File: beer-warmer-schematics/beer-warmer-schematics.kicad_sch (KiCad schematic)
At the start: 38 parts, among them J1 USB_C_Receptacle_USB2.0_14P, J2 Screw_Terminal_01x02, J3 Conn_01x07_Socket, J4 Conn_01x07_Socket, J5 Conn_01x04_Pin, J6 Screw_Terminal_01x03, Q1 AOD4184A, U2 LM2596S-5, U3 CH224K, U4 INA219AxDCN

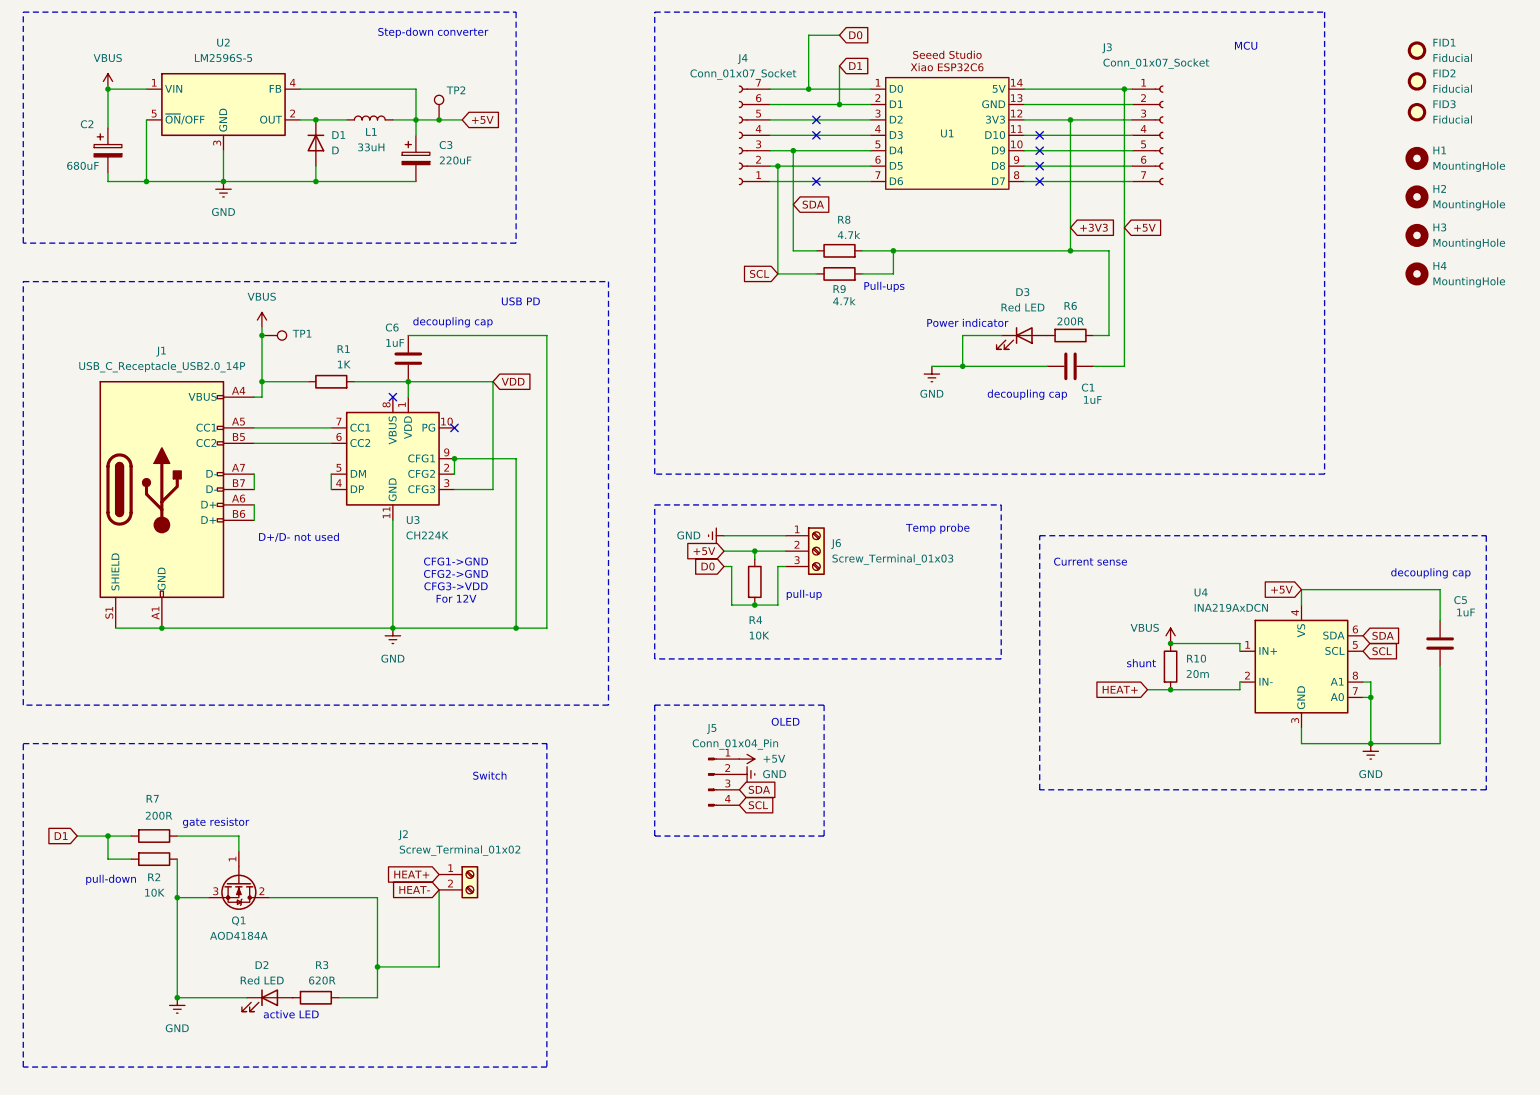
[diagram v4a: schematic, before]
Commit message: fix active led, bottom silkscreen
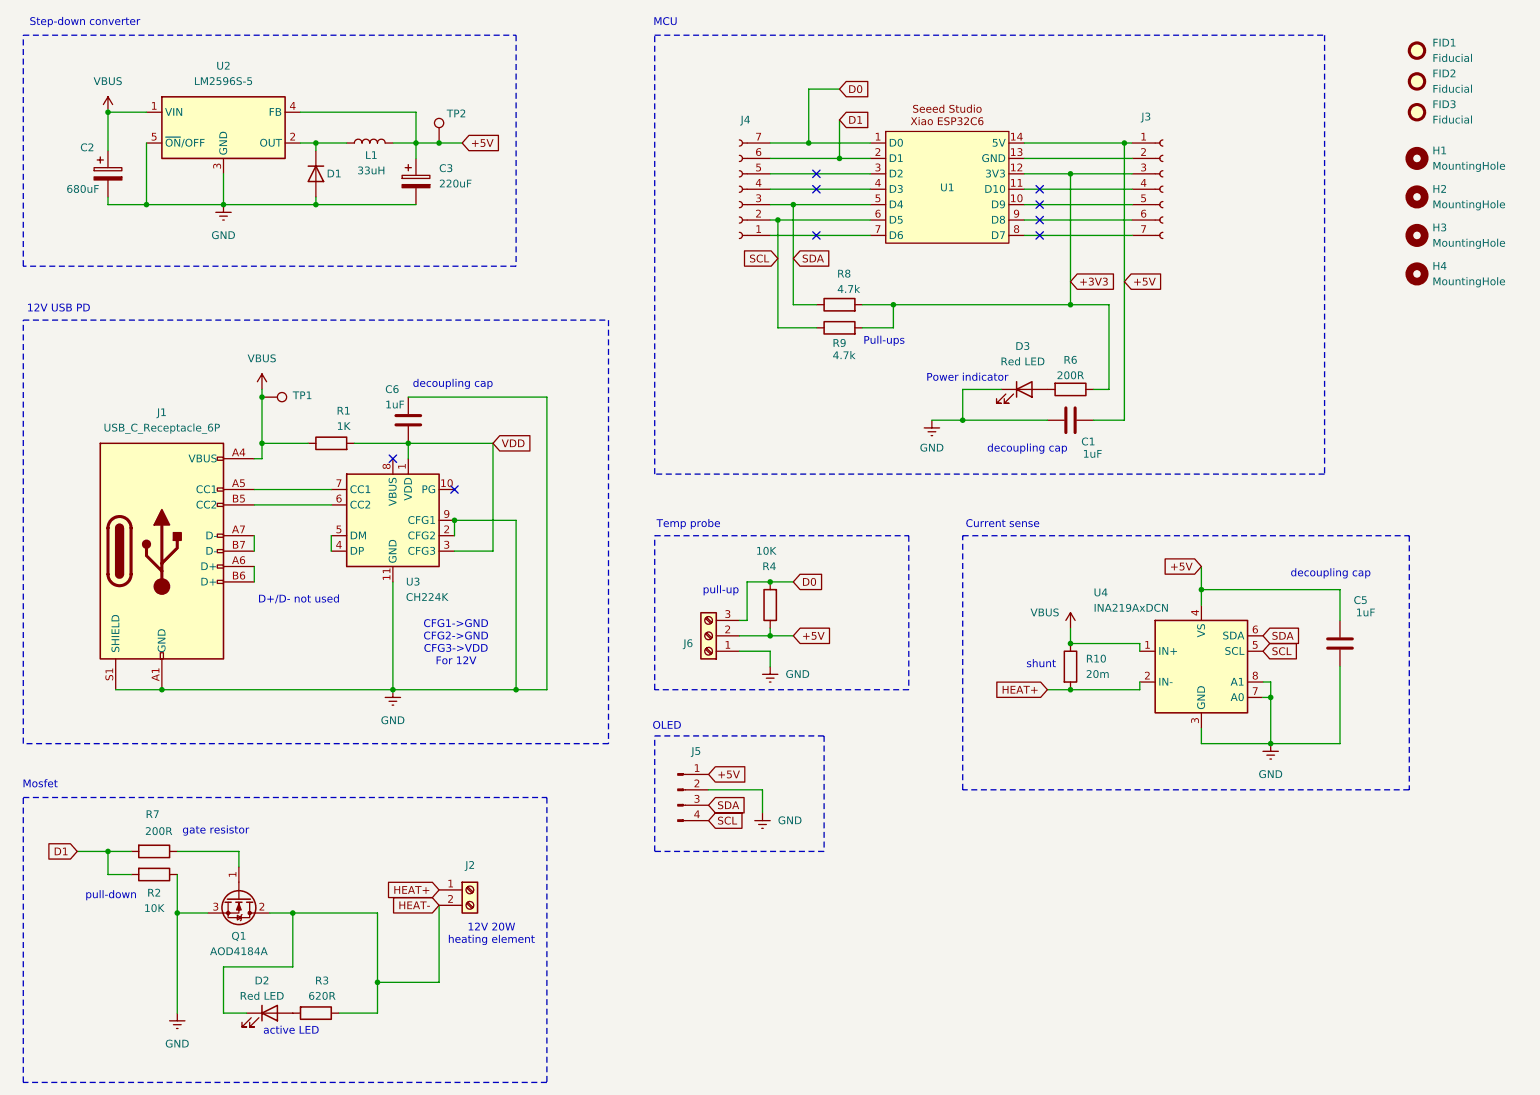
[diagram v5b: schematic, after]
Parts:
- J1: value USB_C_Receptacle_USB2.0_14P -> USB_C_Receptacle_6P
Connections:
- net GND: no longer D2.1 (K)
- net HEAT-: now also D2.1 (K)
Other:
- note added: "12V 20W heating element"
- note added: "12V USB PD"
- note added: "Mosfet"
- note removed: "Switch"
- note removed: "USB PD"
- moved on the sheet: C1, C2, C3, C5, C6, D1, D2, D3, J1, J2, J3, J4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

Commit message: incorporated some feedback
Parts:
- J1: symbol Connector:USB_C_Receptacle_USB2.0_14P -> Connector:USB_C_Receptacle_PowerOnly_6P
- J3, J4: symbol Connector:Conn_01x07_Socket -> Connector_Generic:Conn_01x07
- J5: symbol Connector:Conn_01x04_Pin -> Connector_Generic:Conn_01x04
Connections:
- net D1: now also R2.1; no longer R2.2
- net GND: now also J3.2 (Pin_2), R2.2, U1.13 (GND); no longer J1.A1 (GND), J1.B1 (GND), R2.1
- net SCL: now also R8.1; no longer R9.1
- net SDA: now also R9.1; no longer R8.1
- net VBUS: no longer J1.A4 (VBUS), J1.B4 (VBUS)
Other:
- note removed: "D+/D- not used"
- moved on the sheet: C1, C5, C6, D3, R2, R6, R8, R9, U1

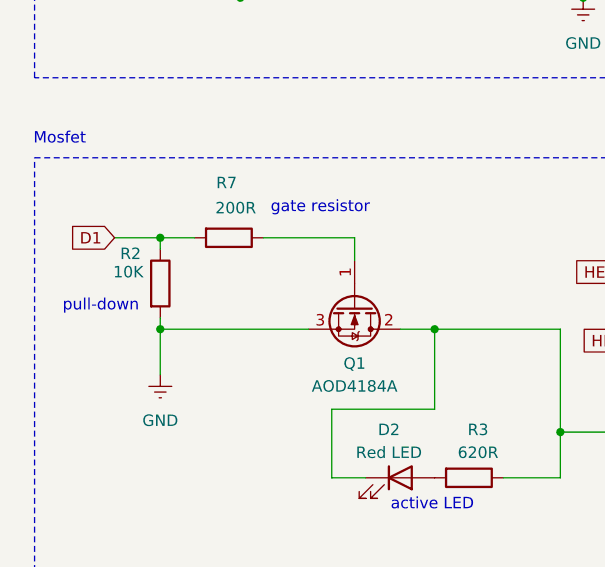
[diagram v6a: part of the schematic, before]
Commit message: low side driver
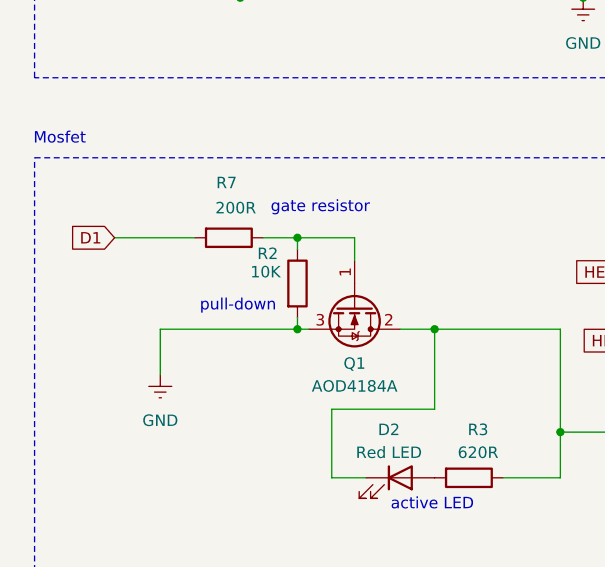
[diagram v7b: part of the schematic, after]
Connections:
- net D1: no longer R2.1
- net at Q1.1 (G), R7.1: now also R2.1
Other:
- moved on the sheet: R2
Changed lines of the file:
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@@
 	(text "pull-down"
 		(exclude_from_sim no)
-		(at 35.306 163.83 0)
+		(at 50.546 163.83 0)
 		(effects
 			(font
@@
 	)
 	(junction
+		(at 57.15 166.37)
+		(diameter 0)
+		(color 0 0 0 0)
+	)
+	(junction
 		(at 96.52 39.37)
 		(diameter 0)
@@
 	)
 	(junction
-		(at 41.91 166.37)
-		(diameter 0)
-		(color 0 0 0 0)
-	)
-	(junction
 		(at 200.66 129.54)
 		(diameter 0)
@@
 	)
 	(junction
-		(at 41.91 156.21)
-		(diameter 0)
-		(color 0 0 0 0)
-	)
-	(junction
 		(at 92.71 39.37)
 		(diameter 0)
@@
 	(junction
 		(at 222.25 113.03)
+		(diameter 0)
+		(color 0 0 0 0)
+	)
+	(junction
+		(at 57.15 156.21)
 		(diameter 0)
 		(color 0 0 0 0)
@@
 	(wire
 		(pts
-			(xy 41.91 165.1) (xy 41.91 166.37)
+			(xy 57.15 165.1) (xy 57.15 166.37)
 		)
 		(stroke
@@
 	(wire
 		(pts
-			(xy 53.34 156.21) (xy 63.5 156.21)
+			(xy 53.34 156.21) (xy 57.15 156.21)
+		)
+		(stroke
+			(width 0)
+			(type default)
+		)
+	)
+	(wire
+		(pts
+			(xy 57.15 156.21) (xy 63.5 156.21)
 		)
 		(stroke
@@
 	(wire
 		(pts
-			(xy 36.83 156.21) (xy 41.91 156.21)
+			(xy 36.83 156.21) (xy 45.72 156.21)
 		)
 		(stroke
@@
 	(wire
 		(pts
-			(xy 41.91 156.21) (xy 45.72 156.21)
-		)
-		(stroke
-			(width 0)
-			(type default)
-		)
-	)
-	(wire
-		(pts
 			(xy 69.85 107.95) (xy 69.85 96.52)
 		)
@@
 	(wire
 		(pts
+			(xy 57.15 166.37) (xy 58.42 166.37)
+		)
+		(stroke
+			(width 0)
+			(type default)
+		)
+	)
+	(wire
+		(pts
 			(xy 82.55 88.9) (xy 91.44 88.9)
 		)
@@
 	(wire
 		(pts
-			(xy 41.91 156.21) (xy 41.91 157.48)
-		)
-		(stroke
-			(width 0)
-			(type default)
-		)
-	)
-	(wire
-		(pts
-			(xy 41.91 166.37) (xy 58.42 166.37)
+			(xy 57.15 156.21) (xy 57.15 157.48)
+		)
+		(stroke
+			(width 0)
+			(type default)
+		)
+	)
+	(wire
+		(pts
+			(xy 41.91 166.37) (xy 57.15 166.37)
 		)
 		(stroke
@@
 	(symbol
 		(lib_id "Device:R")
-		(at 41.91 161.29 0)
+		(at 57.15 161.29 0)
 		(unit 1)
 		(exclude_from_sim no)
@@
 		(dnp no)
 		(property "Reference" "R2"
-			(at 38.608 157.988 0)
+			(at 53.848 157.988 0)
 			(effects
 				(font
@@
 		)
 		(property "Value" "10K"
-			(at 38.354 160.02 0)
+			(at 53.594 160.02 0)
 			(effects
 				(font
@@
 		)
 		(property "Footprint" "Resistor_SMD:R_0603_1608Metric"
-			(at 40.132 161.29 90)
+			(at 55.372 161.29 90)
 			(effects
 				(font
@@
 		)
 		(property "Datasheet" "~"
-			(at 41.91 161.29 0)
+			(at 57.15 161.29 0)
 			(effects
 				(font
@@
 		)
 		(property "Description" "Resistor"
-			(at 41.91 161.29 0)
+			(at 57.15 161.29 0)
 			(effects
 				(font
@@
 		)
 		(property "LCSC" "C15401"
-			(at 41.91 161.29 90)
-			(effects
-				(font
+			(at 57.15 161.29 90)
+			(effects
+				(font

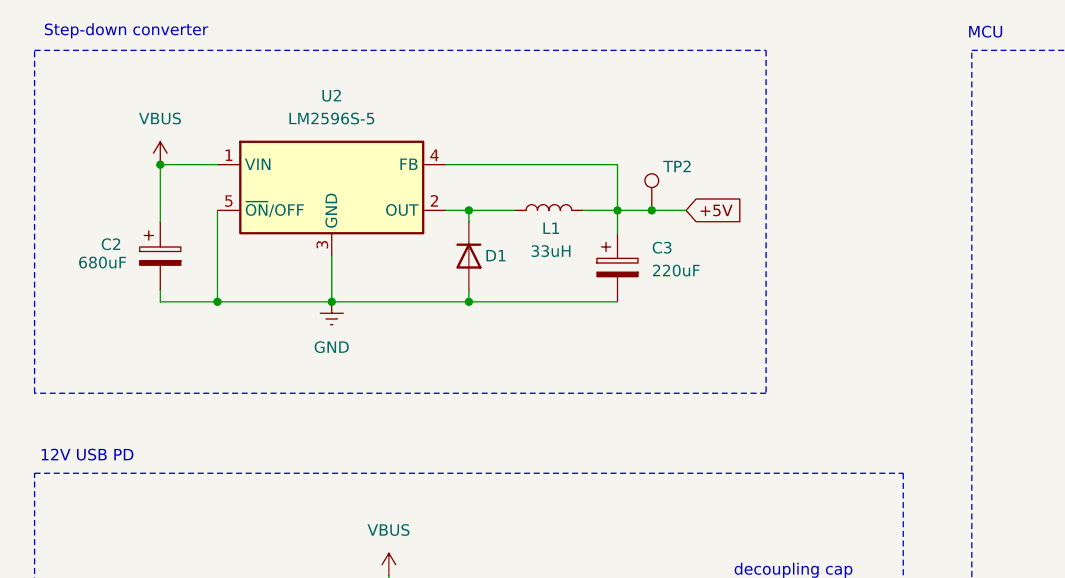
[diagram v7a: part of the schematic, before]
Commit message: different step down
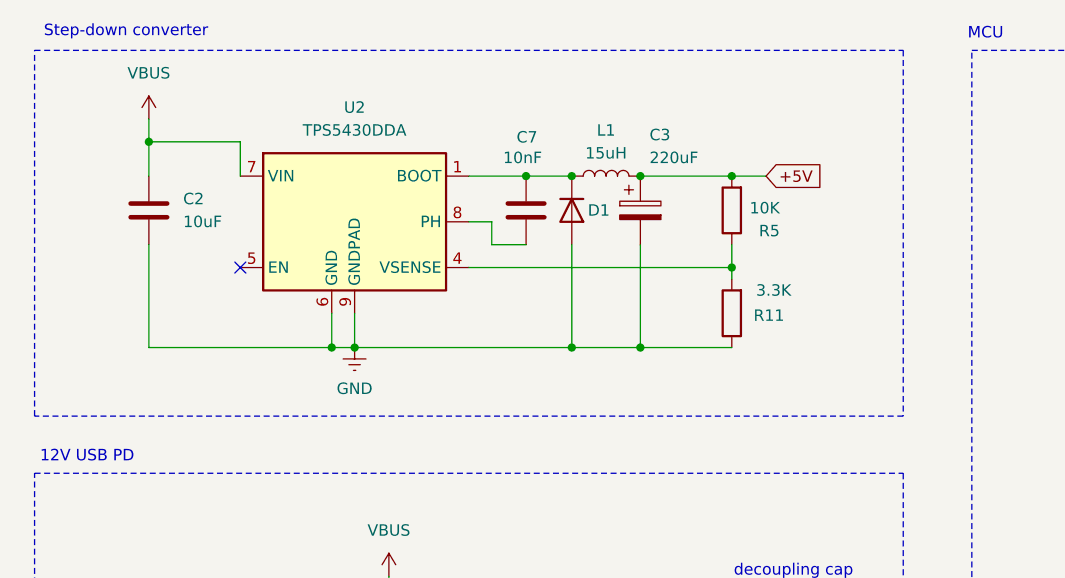
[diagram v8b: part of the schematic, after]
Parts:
- removed C2: 680uF, Capacitor_SMD:CP_Elec_10x10.5, symbol Device:C_Polarized
- removed TP2: TestPoint, TestPoint:TestPoint_Pad_D1.0mm, symbol Connector:TestPoint
- removed U2: LM2596S-5, Package_TO_SOT_SMD:TO-263-5_TabPin3, symbol Regulator_Switching:LM2596S-5
- added C2: 10uF, Capacitor_SMD:C_0805_2012Metric, symbol Device:C
- added C7: 10nF, Capacitor_SMD:C_0402_1005Metric, symbol Device:C
- added R11: 3.3K, Resistor_SMD:R_0603_1608Metric, symbol Device:R
- added R5: 10K, Resistor_SMD:R_0603_1608Metric, symbol Device:R
- added U2: TPS5430DDA, Package_SO:TI_SO-PowerPAD-8_ThermalVias, symbol Regulator_Switching:TPS5430DDA
- L1: value 33uH -> 15uH; footprint Inductor_SMD:L_SXN_SMDRI127 -> Inductor_SMD:L_Changjiang_FNR5040S; LCSC C9400 -> C167969
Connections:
- net +5V: now also R5.2
- net GND: now also C2.2, R11.1, U2.6 (GND), U2.9 (GNDPAD)
- net VBUS: now also C2.1, U2.7 (VIN)
- net at D1.1 (K), L1.1: now also C7.2, U2.1 (BOOT)
- new net: R11.2, R5.1, U2.4 (VSENSE)
- new net: C7.1, U2.8 (PH)
- no-connect marks 9 -> 10
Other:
- moved on the sheet: C3, D1
